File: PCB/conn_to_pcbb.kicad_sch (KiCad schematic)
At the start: 4 parts

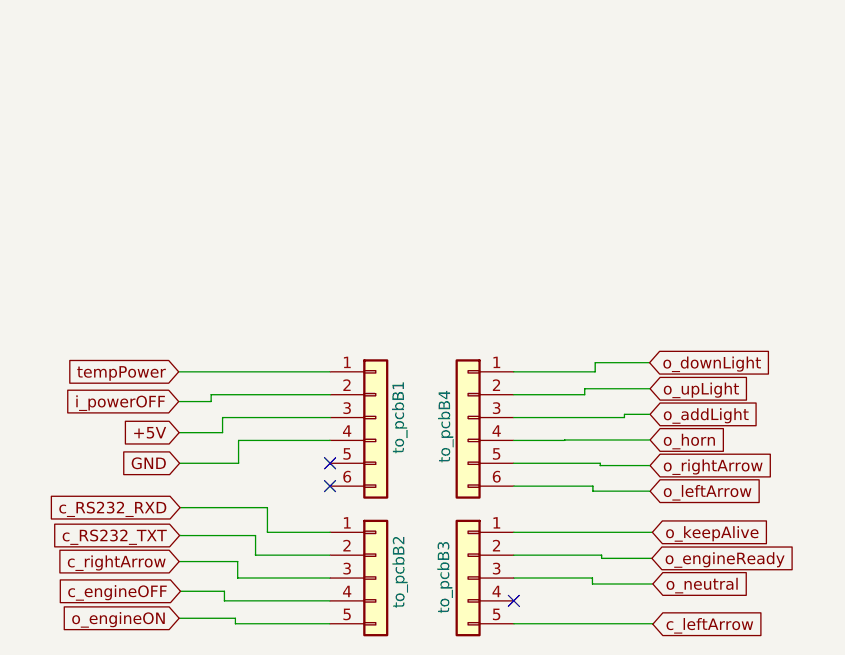
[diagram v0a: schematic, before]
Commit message: Fix and changes for self-power-suppling system
Because the PCB-B should be responsible just for power switching management and PCB-A for the control logic, the
self-power-suppling system has been moved from pcb-b to pcb-a. It should be easier to debug too
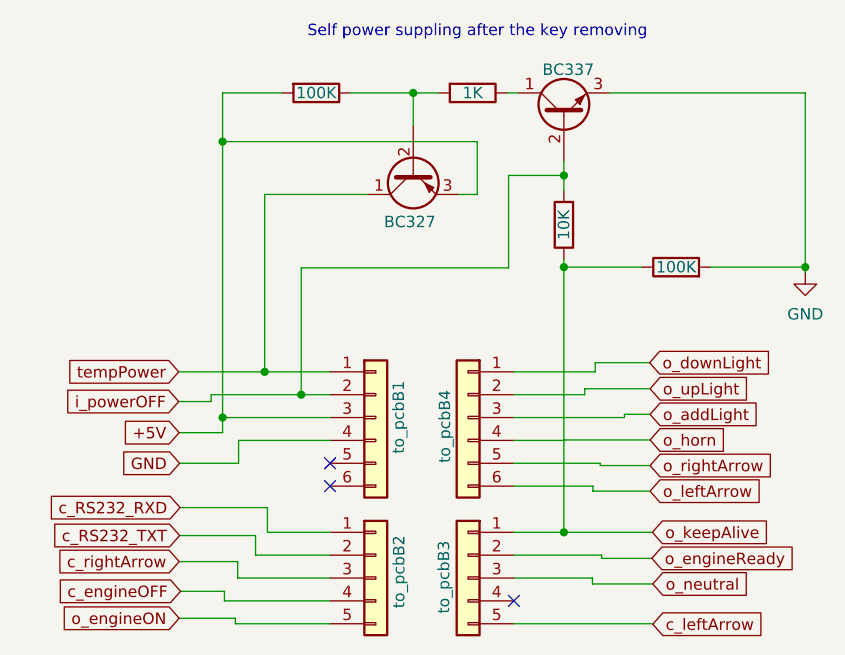
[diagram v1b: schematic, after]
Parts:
- added Q1: BC337, Package_TO_SOT_THT:TO-92L_Inline_Wide, symbol Transistor_BJT:BC337
- added Q2: BC327, Package_TO_SOT_THT:TO-92L_Inline_Wide, symbol Transistor_BJT:BC327
- added RA1, RA3: 100K, Resistor_THT:R_Axial_DIN0207_L6.3mm_D2.5mm_P7.62mm_Horizontal, symbol Device:R
- added RA2: 1K, Resistor_THT:R_Axial_DIN0207_L6.3mm_D2.5mm_P7.62mm_Horizontal, symbol Device:R
- added RA4: 10K, Resistor_THT:R_Axial_DIN0207_L6.3mm_D2.5mm_P7.62mm_Horizontal, symbol Device:R
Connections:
- net +5V: now also Q2.3 (E), RA1.2
- net GND: now also Q1.3 (E), RA3.2
- net i_powerOFF: now also Q1.2 (B), RA4.2
- net o_keepAlive: now also RA3.1, RA4.1
- net tempPower: now also Q2.1 (C)
- new net: Q1.1 (C), RA2.1
- new net: Q2.2 (B), RA1.1, RA2.2
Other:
- note added: "Self power suppling after the key removing"

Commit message: Many changes
- The power drivers component has been implemented with TPCA8120 P-ch MOSfet
- The temp-power management has been moved from pcb-a to pcb-b
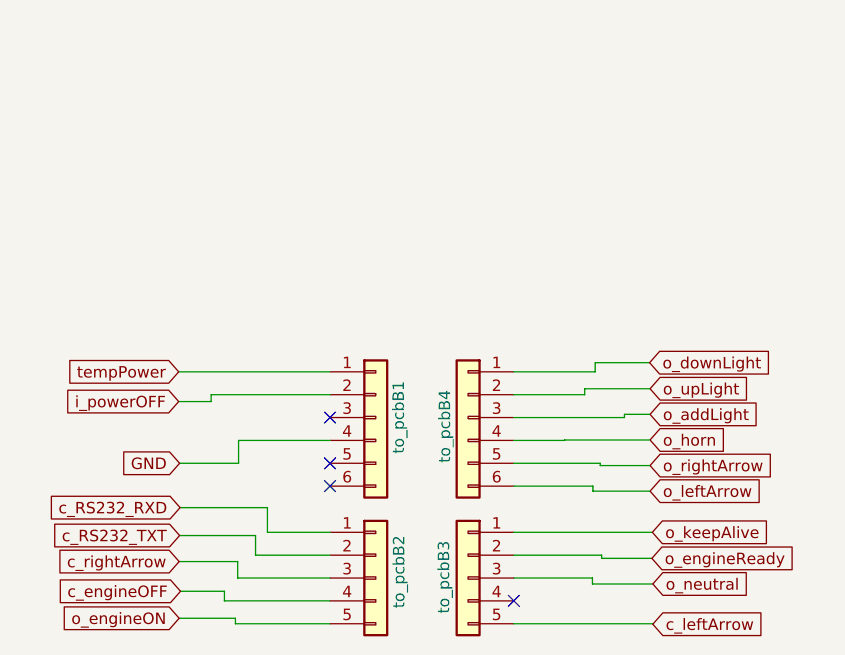
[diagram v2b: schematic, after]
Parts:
- removed Q1: BC337, Package_TO_SOT_THT:TO-92L_Inline_Wide, symbol Transistor_BJT:BC337
- removed Q2: BC327, Package_TO_SOT_THT:TO-92L_Inline_Wide, symbol Transistor_BJT:BC327
- removed RA1, RA3: 100K, Resistor_THT:R_Axial_DIN0207_L6.3mm_D2.5mm_P7.62mm_Horizontal, symbol Device:R
- removed RA2: 1K, Resistor_THT:R_Axial_DIN0207_L6.3mm_D2.5mm_P7.62mm_Horizontal, symbol Device:R
- removed RA4: 10K, Resistor_THT:R_Axial_DIN0207_L6.3mm_D2.5mm_P7.62mm_Horizontal, symbol Device:R
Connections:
- net +5V: no longer names the net of to_pcbB1.3 (Pin_3)
- no-connect marks 3 -> 4
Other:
- note removed: "Self power suppling after the key removing"

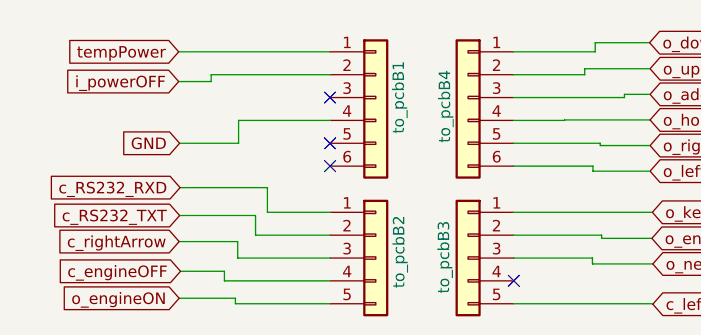
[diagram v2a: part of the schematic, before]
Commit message: PCB-A size reducing
Now PCB-B and PCB-A fits almost perfectly, but not the pin-header connectors. I will use wires instead. But they can be mnounted A on top of B ;-)
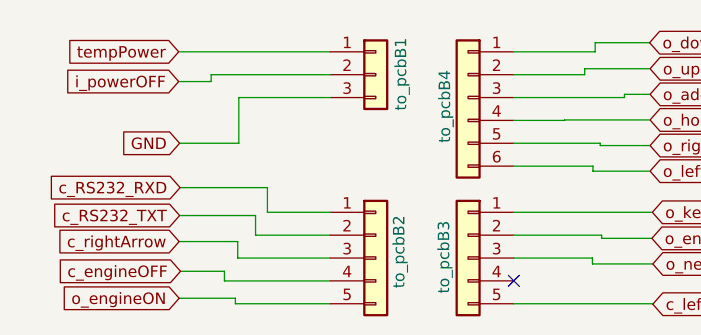
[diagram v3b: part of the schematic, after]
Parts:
- removed to_pcbB1: Conn_01x06, Connector_PinHeader_2.54mm:PinHeader_1x06_P2.54mm_Vertical, symbol Connector_Generic:Conn_01x06
- added to_pcbB1: Conn_01x03, Connector_PinHeader_2.54mm:PinHeader_1x03_P2.54mm_Vertical, symbol Connector_Generic:Conn_01x03
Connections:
- net GND: now also to_pcbB1.3 (Pin_3)
- net i_powerOFF: now also to_pcbB1.2 (Pin_2)
- net tempPower: now also to_pcbB1.1 (Pin_1)
- no-connect marks 4 -> 1
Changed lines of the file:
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@@
     (comment 2 "Connectors to the PCB-A")
   )
-  (no_connect (at 115.1128 77.5208))
   (no_connect (at 135.5344 92.8116))
-  (no_connect (at 115.1128 80.0608))
-  (no_connect (at 115.1128 72.4408))
   (wire (pts (xy 106.8324 85.5472) (xy 106.8324 87.7316))
     (stroke (width 0) (type default))
@@
     (stroke (width 0) (type default))
   )
-  (wire (pts (xy 98.3996 77.5208) (xy 104.9528 77.5208))
+  (wire (pts (xy 98.3996 77.5208) (xy 104.9782 77.5208))
     (stroke (width 0) (type default))
   )
@@
     (stroke (width 0) (type default))
   )
-  (wire (pts (xy 104.9528 77.5208) (xy 104.9528 74.9808))
+  (wire (pts (xy 104.9782 77.5208) (xy 104.9782 72.4408))
     (stroke (width 0) (type default))
   )
@@
     (stroke (width 0) (type default))
   )
-  (wire (pts (xy 104.9528 74.9808) (xy 115.1128 74.9808))
+  (wire (pts (xy 104.9782 72.4408) (xy 115.1128 72.4408))
     (stroke (width 0) (type default))
   )
@@
     )
   )
-  (symbol (lib_id "Connector_Generic:Conn_01x06") (at 120.1928 72.4408 0) (unit 1)
+  (symbol (lib_id "Connector_Generic:Conn_01x03") (at 120.1928 69.9008 0) (unit 1)
     (in_bom yes) (on_board yes) (dnp no)
-    (property "Reference" "to_pcbB1" (at 122.7328 76.454 90)
+    (property "Reference" "to_pcbB1" (at 122.9868 73.8886 90)
       (effects (font (size 1.27 1.27)) (justify left))
     )
-    (property "Value" "Conn_01x06" (at 123.19 74.9807 0)
-      (effects (font (size 1.27 1.27)) (justify left) hide)
-    )
-    (property "Footprint" "Connector_PinHeader_2.54mm:PinHeader_1x06_P2.54mm_Vertical" (at 120.1928 72.4408 0)
-      (effects (font (size 1.27 1.27)) hide)
-    )
-    (property "Datasheet" "~" (at 120.1928 72.4408 0)
-      (effects (font (size 1.27 1.27)) hide)
-    )
+    (property "Value" "Conn_01x03" (at 122.7328 71.1708 0)
+      (effects (font (size 1.27 1.27)) (justify left) hide)
+    )
+    (property "Footprint" "Connector_PinHeader_2.54mm:PinHeader_1x03_P2.54mm_Vertical" (at 120.1928 69.9008 0)
+      (effects (font (size 1.27 1.27)) hide)
+    )
+    (property "Datasheet" "~" (at 120.1928 69.9008 0)
+      (effects (font (size 1.27 1.27)) hide)
+    )
+    (pin "3")
+    (pin "2")
     (pin "1")
-    (pin "2")
-    (pin "3")
-    (pin "4")
-    (pin "5")
-    (pin "6")
     (instances
       (project "pcb-a"

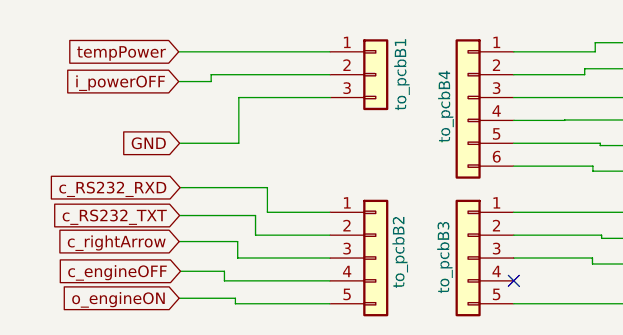
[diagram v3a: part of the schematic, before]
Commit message: Size reducing and component rationalization
- RS232(TTL) lines on PCB-B have been removed (MAX232 is already mounted in PCB-A)
- The two PCB can no more be connected using pin-header connectors. You have to use welded wires, now.
  (this solution is not beautiful as the original, but it is a more flexible one and it also allowd me
  to reduce the PCB size)

The PCBs size is approximately 109.7mm x 43.5mm.
For this dual-face sigle-layer (THT) version this is the minimum size I can achieve.
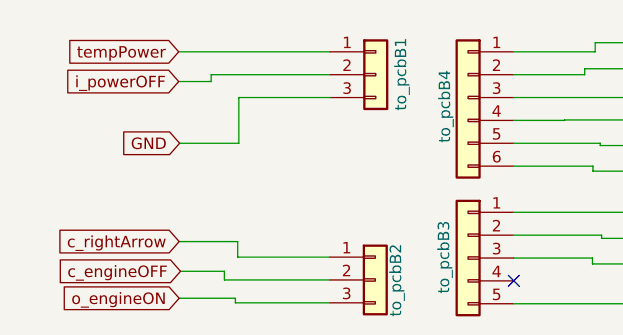
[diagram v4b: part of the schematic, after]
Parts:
- removed to_pcbB2: Conn_01x05, Connector_PinHeader_2.54mm:PinHeader_1x05_P2.54mm_Vertical, symbol Connector_Generic:Conn_01x05
- added to_pcbB2: Conn_01x03, Connector_PinHeader_2.54mm:PinHeader_1x03_P2.54mm_Vertical, symbol Connector_Generic:Conn_01x03
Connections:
- net c_engineOFF: now also to_pcbB2.2 (Pin_2)
- net c_rightArrow: now also to_pcbB2.1 (Pin_1)
- net o_engineON: now also to_pcbB2.3 (Pin_3)

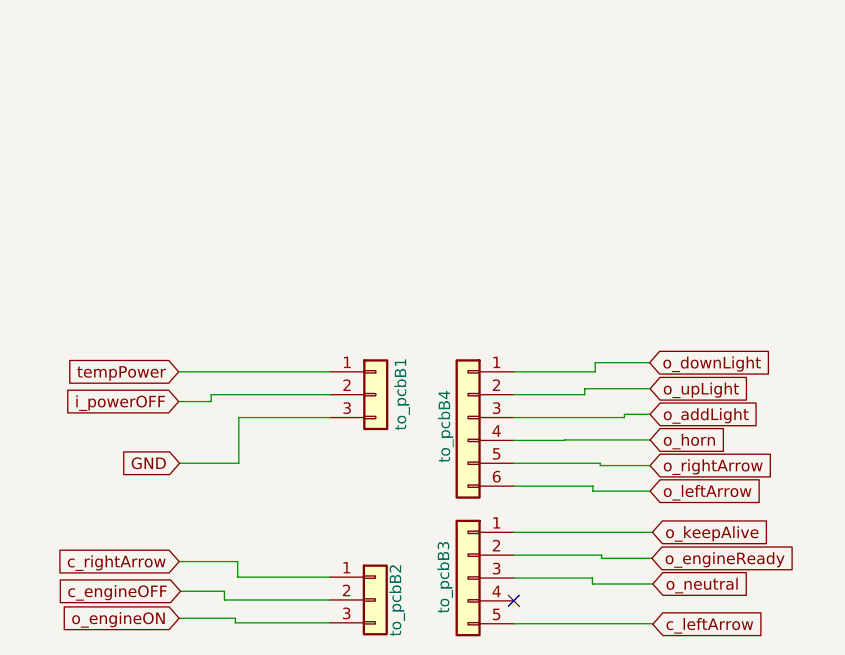
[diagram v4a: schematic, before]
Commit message: Pin-header connectors adjustment
The main idea to mount the two pcb-A on the pcbB has been dropped, because the result is a too much chatic one and I realized that
wires welder on the top is a dangerous solution, they can create unwanted contacts and short-circuits... So, I choise to place the
two PCB beside. So, in order to get a more ordered and clean solution, I am using flat cables instead wires, and pin-header
connectors instead of welding them directly. I foung good connectors where every female-plug is blocked in its male-socket. But,
they are available just for even numbers of pins. For this reason, I have adjusted all the pin-header connectors and their
positions.
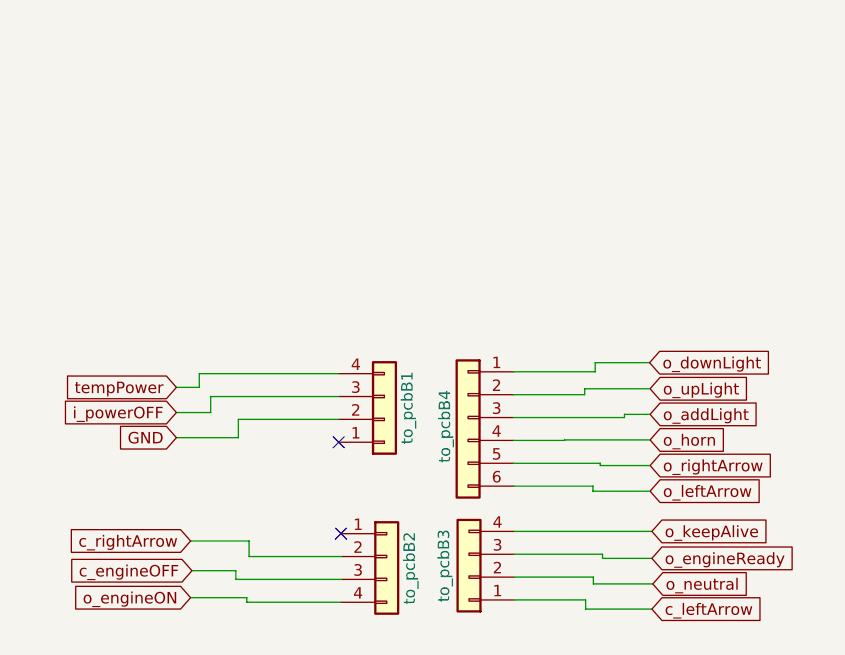
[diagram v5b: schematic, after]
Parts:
- removed to_pcbB1, to_pcbB2: Conn_01x03, Connector_PinHeader_2.54mm:PinHeader_1x03_P2.54mm_Vertical, symbol Connector_Generic:Conn_01x03
- removed to_pcbB3: Conn_01x05, Connector_PinHeader_2.54mm:PinHeader_1x05_P2.54mm_Vertical, symbol Connector_Generic:Conn_01x05
- added to_pcbB1, to_pcbB2, to_pcbB3: Conn_01x04, Connector_PinHeader_2.54mm:PinHeader_1x04_P2.54mm_Vertical, symbol Connector_Generic:Conn_01x04
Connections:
- net GND: now also to_pcbB1.2 (Pin_2)
- net c_engineOFF: now also to_pcbB2.3 (Pin_3)
- net c_leftArrow: now also to_pcbB3.1 (Pin_1)
- net c_rightArrow: now also to_pcbB2.2 (Pin_2)
- net i_powerOFF: now also to_pcbB1.3 (Pin_3)
- net o_engineON: now also to_pcbB2.4 (Pin_4)
- net o_engineReady: now also to_pcbB3.3 (Pin_3)
- net o_keepAlive: now also to_pcbB3.4 (Pin_4)
- net o_neutral: now also to_pcbB3.2 (Pin_2)
- net tempPower: now also to_pcbB1.4 (Pin_4)
- no-connect marks 1 -> 2

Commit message: Bike-stand switch moved in the rear-connector
All connectors have been placed in one single sheet
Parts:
- removed to_pcbB1, to_pcbB2, to_pcbB3: Conn_01x04, Connector_PinHeader_2.54mm:PinHeader_1x04_P2.54mm_Vertical, symbol Connector_Generic:Conn_01x04
- removed to_pcbB4: Conn_01x06, Connector_PinHeader_2.54mm:PinHeader_1x06_P2.54mm_Vertical, symbol Connector_Generic:Conn_01x06
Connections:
- no-connect marks 2 -> 0
